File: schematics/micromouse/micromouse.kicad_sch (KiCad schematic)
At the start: 0 parts

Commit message: Update
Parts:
- added J1: TOF_FRONT, Connector_PinHeader_2.54mm:PinHeader_1x06_P2.54mm_Vertical, symbol Connector_Generic:Conn_01x06
- added J2: TOF_LEFT, Connector_PinHeader_2.54mm:PinHeader_1x06_P2.54mm_Vertical, symbol Connector_Generic:Conn_01x06
- added J3: TOF_RIGHT, Connector_PinHeader_2.54mm:PinHeader_1x06_P2.54mm_Vertical, symbol Connector_Generic:Conn_01x06
- added J4: Conn_01x06, Connector_PinHeader_2.54mm:PinHeader_1x06_P2.54mm_Vertical, symbol Connector_Generic:Conn_01x06
- added J5: BatteryConnector, Connector_JST:JST_EH_B2B-EH-A_1x02_P2.50mm_Vertical, symbol Connector_Generic:Conn_01x02
- added U1: STM32F103CBTx, Package_QFP:LQFP-48_7x7mm_P0.5mm, symbol MCU_ST_STM32F1:STM32F103CBTx
- added U2: PMW3360DM-T2QU, PMW3360DM:PMW3360, symbol PMW3360DM:PMW3360DM-T2QU
- added U3: BMI160, Package_LGA:Bosch_LGA-14_3x2.5mm_P0.5mm, symbol Sensor_Motion:BMI160
- added Y1: Crystal, Crystal:Crystal_HC49-4H_Vertical, symbol Device:Crystal
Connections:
- new net: U1.23 (VSS), U1.35 (VSS), U1.47 (VSS)
- new net +3.3V: J1.6 (Pin_6), J2.6 (Pin_6), J3.6 (Pin_6), J4.5 (Pin_5)
- new net GND: J1.5 (Pin_5), J2.5 (Pin_5), J3.5 (Pin_5), J4.4 (Pin_4)
- new net bt_enable: J4.6 (Pin_6)
- new net bt_rx: J4.2 (Pin_2)
- new net bt_state: J4.1 (Pin_1)
- new net bt_tx: J4.3 (Pin_3)
- new net tofF_int: J1.2 (Pin_2)
- new net tofF_scl: J1.3 (Pin_3)
- new net tofF_sda: J1.4 (Pin_4)
- new net tofF_xshut: J1.1 (Pin_1)
- new net tofL_int: J2.2 (Pin_2)
- new net tofL_scl: J2.3 (Pin_3)
- new net tofL_sda: J2.4 (Pin_4)
- new net tofL_xshut: J2.1 (Pin_1)
- new net tofR_int: J3.2 (Pin_2)
- new net tofR_scl: J3.3 (Pin_3)
- new net tofR_sda: J3.4 (Pin_4)
- new net tofR_xshut: J3.1 (Pin_1)

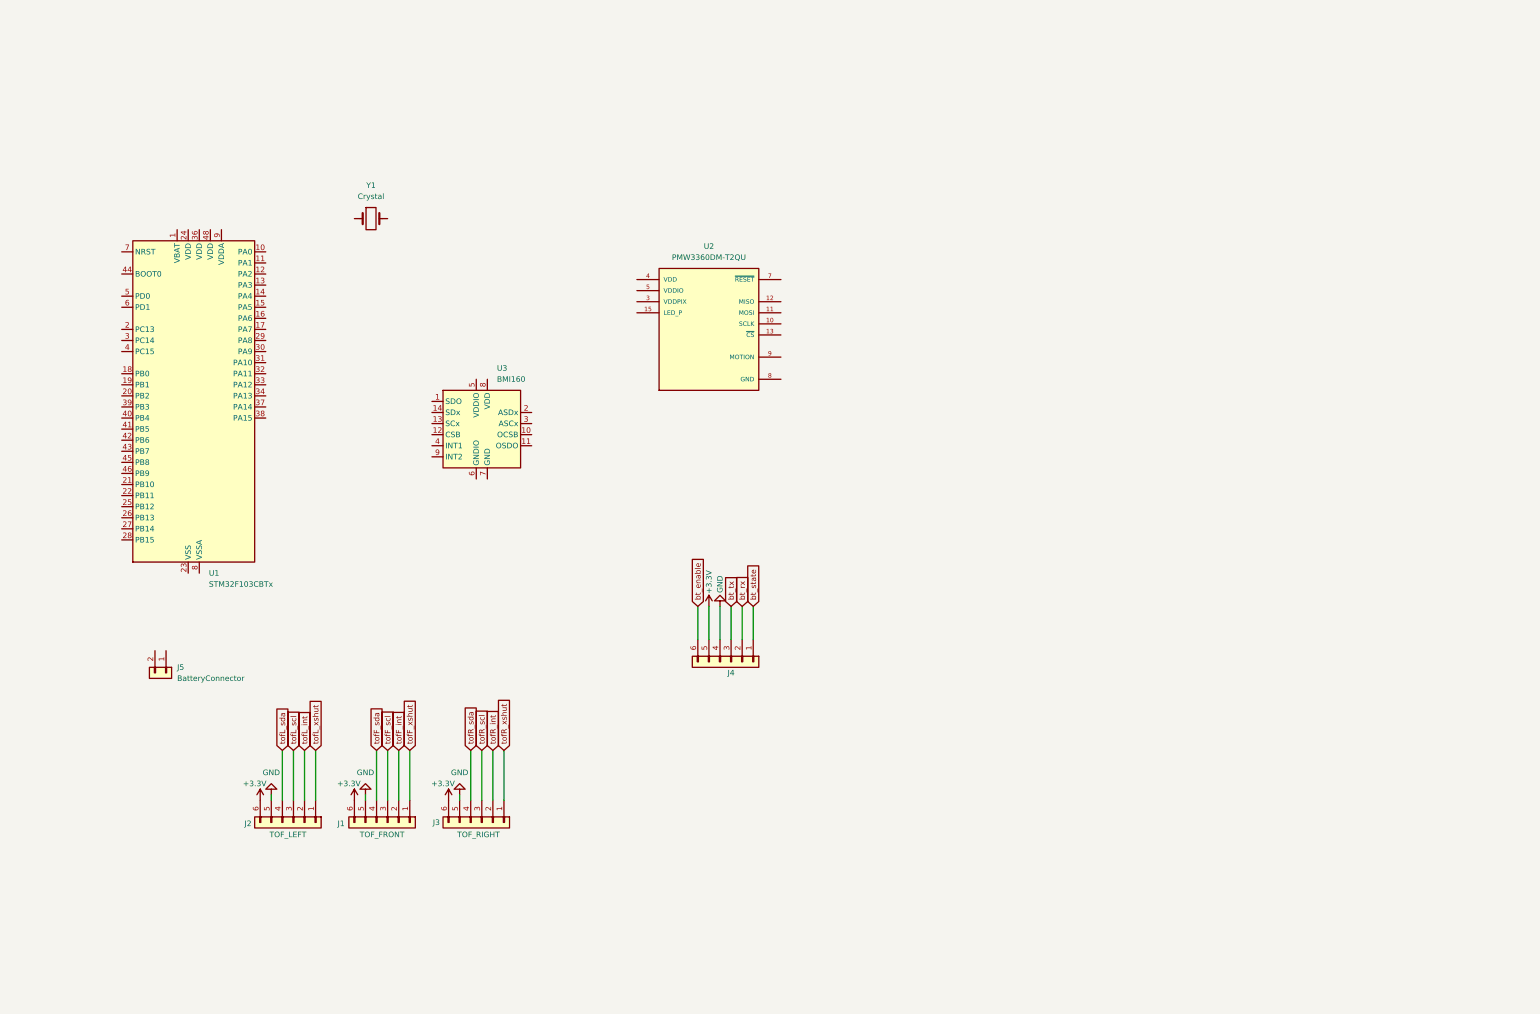
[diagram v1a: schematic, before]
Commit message: Move datasheets, add application note for smt32f103 hardware development Add PCB cut from 3D model (DXF) Reorganize datasheet, add labels and connectors for tofs i2c (x2), add I2C expancer (PCF8574), add mouse sensor (PMW3360) connector and SPI1 labels Added SPI2 labels (may be removed if not used)
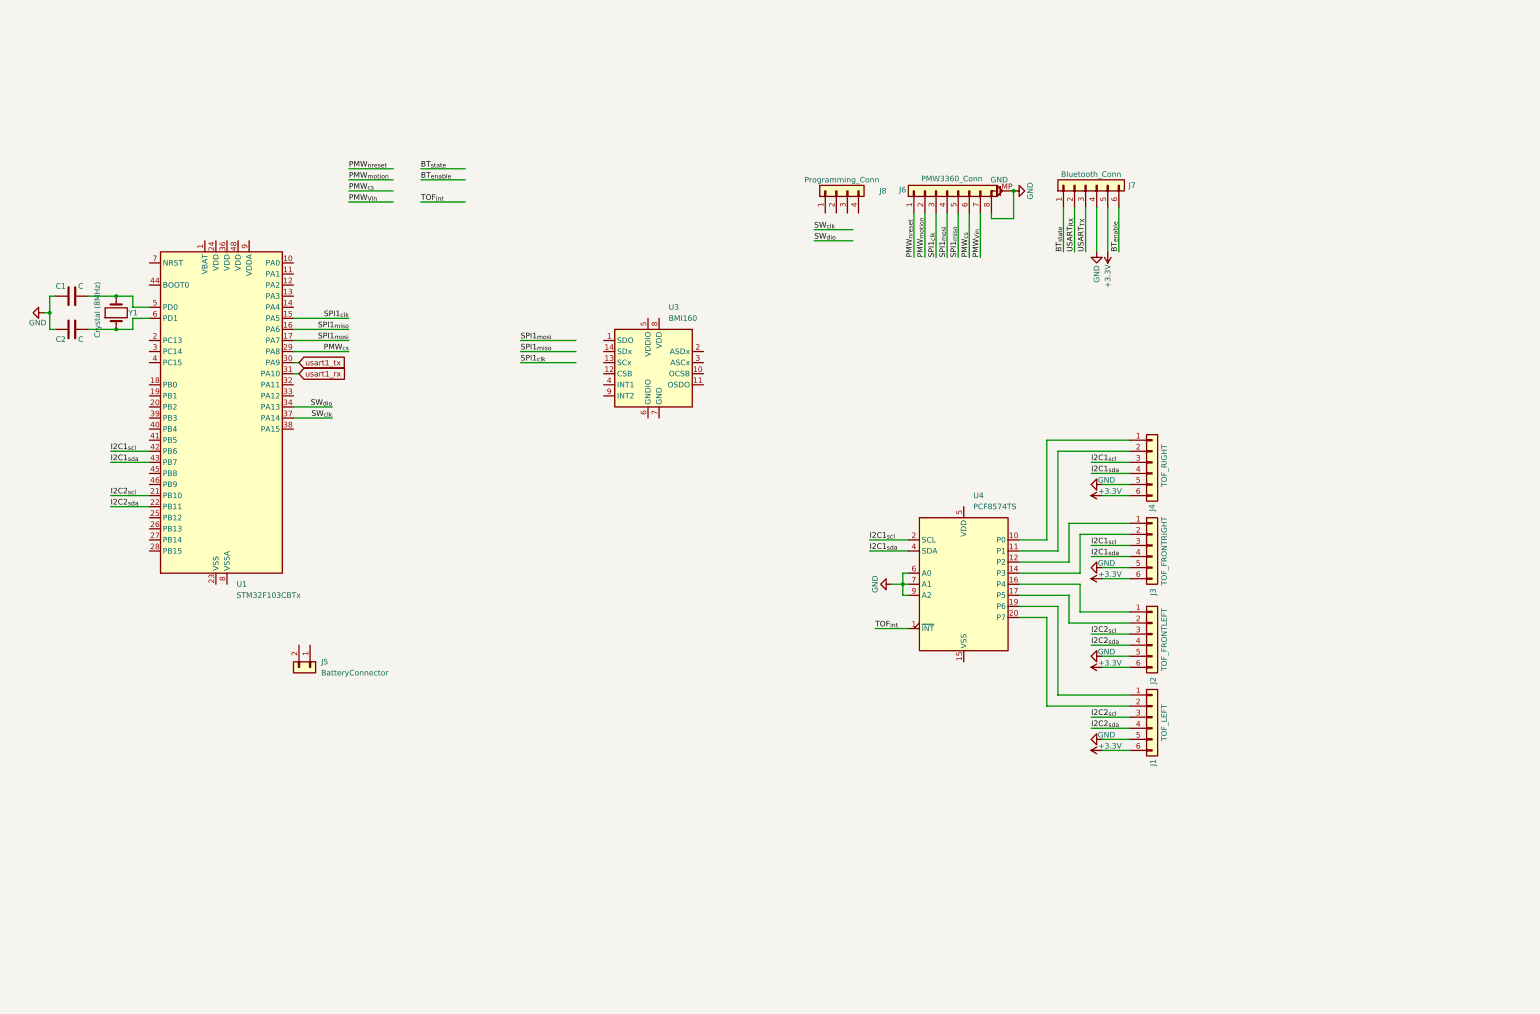
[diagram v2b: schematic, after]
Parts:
- removed U2: PMW3360DM-T2QU, PMW3360DM:PMW3360, symbol PMW3360DM:PMW3360DM-T2QU
- added C1, C2: C, symbol Device:C
- added J3: TOF_FRONTRIGHT, Connector_PinHeader_2.54mm:PinHeader_1x06_P2.54mm_Vertical, symbol Connector_Generic:Conn_01x06
- added J6: PMW3360_Conn, Connector_JST:JST_SH_SM08B-SRSS-TB_1x08-1MP_P1.00mm_Horizontal, symbol Connector_Generic_MountingPin:Conn_01x08_MountingPin
- added J8: Programming_Conn, Connector_PinHeader_2.54mm:PinHeader_1x06_P2.54mm_Vertical, symbol Connector_Generic:Conn_01x04
- added U4: PCF8574TS, Package_SO:SSOP-20_4.4x6.5mm_P0.65mm, symbol Interface_Expansion:PCF8574TS
- J1: value TOF_FRONT -> TOF_LEFT
- J2: value TOF_LEFT -> TOF_FRONTLEFT
- J7: renamed from J4; value Conn_01x06 -> Bluetooth_Conn
- Y1: value Crystal -> Crystal (8MHz)
- renumbered J3 to J4
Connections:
- net tofF_scl is gone; now on net I2C2_{scl}: J1.3 (Pin_3)
- net tofF_sda is gone; now on net I2C2_{sda}: J1.4 (Pin_4)
- net tofL_scl is gone; now on net I2C2_{scl}: J2.3 (Pin_3)
- net tofL_sda is gone; now on net I2C2_{sda}: J2.4 (Pin_4)
- net tofR_scl is gone; now on net I2C1_{scl}: J4.3 (Pin_3)
- net tofR_sda is gone; now on net I2C1_{sda}: J4.4 (Pin_4)
- net +3.3V: now also J3.6 (Pin_6)
- net GND: now also C1.1, C2.2, J3.5 (Pin_5), J6.8 (Pin_8), J6.MP (MountPin), U4.6 (A0), U4.7 (A1), U4.9 (A2)
- net SPI1_{clk}: now reaches U1.15 (PA5)
- net SPI1_{clk}: now also J6.3 (Pin_3)
- net SPI1_{miso}: now reaches U1.16 (PA6)
- net SPI1_{miso}: now also J6.5 (Pin_5)
- net SPI1_{mosi}: now reaches U1.17 (PA7)
- net SPI1_{mosi}: now also J6.4 (Pin_4)
- net I2C2_{scl}: now reaches U1.21 (PB10)
- net I2C2_{sda}: now reaches U1.22 (PB11)
- net PMW_{cs}: now reaches U1.29 (PA8)
- net PMW_{cs}: now also J6.6 (Pin_6)
- net usart1_tx: now reaches U1.30 (PA9)
- net usart1_rx: now reaches U1.31 (PA10)
- net SW_{dio}: now reaches U1.34 (PA13)
- net SW_{clk}: now reaches U1.37 (PA14)
- net I2C1_{scl}: now reaches U1.42 (PB6)
- net I2C1_{scl}: now also J3.3 (Pin_3), U4.2 (SCL)
- net I2C1_{sda}: now reaches U1.43 (PB7)
- net I2C1_{sda}: now also J3.4 (Pin_4), U4.4 (SDA)
- net at U1.5 (PD0): now also Y1.2, C1.2
- net at U1.6 (PD1): now also Y1.1, C2.1
- net bt_enable renamed BT_{enable}
- net bt_rx renamed USART_{RX}
- net bt_state renamed BT_{state}
- net bt_tx renamed USART_{TX}
- net tofF_int: no longer names the net of J1.2 (Pin_2)
- net tofF_int: now also U4.20 (P7)
- net tofF_xshut: no longer names the net of J1.1 (Pin_1)
- net tofF_xshut: now also U4.19 (P6)
- net tofL_int: no longer names the net of J2.2 (Pin_2)
- net tofL_int: now also U4.17 (P5)
- net tofL_xshut: no longer names the net of J2.1 (Pin_1)
- net tofL_xshut: now also U4.16 (P4)
- net tofR_int: no longer names the net of J4.2 (Pin_2)
- net tofR_int: now also U4.11 (P1)
- net tofR_xshut: no longer names the net of J4.1 (Pin_1)
- net tofR_xshut: now also U4.10 (P0)
- new net: J3.1 (Pin_1), U4.12 (P2)
- new net: J3.2 (Pin_2), U4.14 (P3)
- new net PMW_{Vin}: J6.7 (Pin_7)
- new net PMW_{motion}: J6.2 (Pin_2)
- new net PMW_{nreset}: J6.1 (Pin_1)
- new net TOF_{int}: U4.1 (~{INT})
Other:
- moved on the sheet: J4, J5, J7, U1, U3, Y1

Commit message: Reorganize again... add things
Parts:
- removed U3: BMI160, Package_LGA:Bosch_LGA-14_3x2.5mm_P0.5mm, symbol Sensor_Motion:BMI160
- added D1: LED, symbol Device:LED
- added H1, H2, H3, H4: MountingHole_Pad, MountingHole:MountingHole_2.2mm_M2_ISO14580_Pad, symbol Mechanical:MountingHole_Pad
- added J10: MotorB_Conn, Connector_JST:JST_EH_B2B-EH-A_1x02_P2.50mm_Vertical, symbol Connector_Generic:Conn_01x02
- added J11: BMI_ConnB, Connector_PinHeader_2.54mm:PinHeader_1x07_P2.54mm_Vertical, symbol Connector_Generic:Conn_01x07
- added J12: BMI_ConnA, Connector_PinHeader_2.54mm:PinHeader_1x05_P2.54mm_Vertical, symbol Connector_Generic:Conn_01x05
- added J9: MotorA_Conn, Connector_JST:JST_EH_B2B-EH-A_1x02_P2.50mm_Vertical, symbol Connector_Generic:Conn_01x02
- added SW1: SW_Push, symbol Switch:SW_Push
- added SW2: SW_SPDT, symbol Switch:SW_SPDT
- added U2: DRV8833PWP, Package_SO:HTSSOP-16-1EP_4.4x5mm_P0.65mm_EP3.4x5mm_Mask2.46x2.31mm_ThermalVias, symbol Driver_Motor:DRV8833PWP
- C1, C2: footprint (none) -> Capacitor_SMD:C_0805_2012Metric_Pad1.18x1.45mm_HandSolder
- J6: footprint Connector_JST:JST_SH_SM08B-SRSS-TB_1x08-1MP_P1.00mm_Horizontal -> Connector_JST:JST_SH_BM08B-SRSS-TB_1x08-1MP_P1.00mm_Vertical
- J8: footprint Connector_PinHeader_2.54mm:PinHeader_1x06_P2.54mm_Vertical -> Connector_PinHeader_2.54mm:PinHeader_1x04_P2.54mm_Vertical
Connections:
- net PMW_{Vin} is gone; now on net VCC_{3.3}: J6.7 (Pin_7)
- net GND: now also U4.15 (VSS), H1.1, H2.1, H3.1, H4.1, J11.3 (Pin_3), U2.13 (GND), U2.17 (GND)
- net SPI1_{clk}: now also J11.4 (Pin_4)
- net SPI1_{miso}: now also J11.7 (Pin_7)
- net SPI1_{mosi}: now also J11.5 (Pin_5)
- net +3.3V renamed VCC_{3.3}
- net VCC_{3.3}: now also J11.1 (Pin_1)
- net usart1_rx renamed USART1_{RX}
- net usart1_tx renamed USART1_{TX}
- new net: J9.1 (Pin_1), U2.2 (AOUT1)
- new net: J9.2 (Pin_2), U2.4 (AOUT2)
- new net: J10.2 (Pin_2), U2.5 (BOUT2)
- new net: J10.1 (Pin_1), U2.7 (BOUT1)
- new net BMI_{cs}: J11.6 (Pin_6)
- new net BMI_{int1}: J12.3 (Pin_3)
- new net BMI_{int2}: J12.2 (Pin_2)
- new net MOTOR_{a1}: U2.16 (AIN1)
- new net MOTOR_{a2}: U2.15 (AIN2)
- new net MOTOR_{aen}: U2.3 (AISEN)
- new net MOTOR_{b1}: U2.9 (BIN1)
- new net MOTOR_{b2}: U2.10 (BIN2)
- new net MOTOR_{ben}: U2.6 (BISEN)
- new net MOTOR_{fault}: U2.8 (~{FAULT})
- new net MOTOR_{sleep}: U2.1 (~{SLEEP})
- new net VCC_{6}: U2.12 (VM)
- no-connect marks 0 -> 4
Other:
- note added: "PMW3360 Mounting Holes"
- moved on the sheet: J1, J2, J3, J4, J5

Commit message: Schamatic status update: * STM32 with external clock, DebugPort and communication lines (SPI1, I2C0 and I2C1) * First version of power supply schematic [TODO: Check possible short circuit] * Motor controller schematic * Mouse sensor connector + mounting holes * Bluetooth connector for HC-05/HC-06 * TOF schematic using GPIO expander * BMI160 Mounting holes
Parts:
- added C3: 0.01uF, Capacitor_SMD:C_0805_2012Metric_Pad1.18x1.45mm_HandSolder, symbol Device:C
- added C4: 10uF, Capacitor_SMD:C_0805_2012Metric_Pad1.18x1.45mm_HandSolder, symbol Device:C
- added C5: 2.2uF, Capacitor_SMD:C_0805_2012Metric_Pad1.18x1.45mm_HandSolder, symbol Device:C
- added J13: StepDown_{In+}, Connector_PinHeader_2.54mm:PinHeader_1x01_P2.54mm_Vertical, symbol Connector_Generic:Conn_01x01
- added J14: StepDown_{In-}, Connector_PinHeader_2.54mm:PinHeader_1x01_P2.54mm_Vertical, symbol Connector_Generic:Conn_01x01
- added J15: StepDown_{Out+}, Connector_PinHeader_2.54mm:PinHeader_1x01_P2.54mm_Vertical, symbol Connector_Generic:Conn_01x01
- added J16: StepDown_{Out-}, Connector_PinHeader_2.54mm:PinHeader_1x01_P2.54mm_Vertical, symbol Connector_Generic:Conn_01x01
- added R1: R, Resistor_SMD:R_0805_2012Metric_Pad1.20x1.40mm_HandSolder, symbol Device:R
- added R2, R3: 200m, Resistor_SMD:R_0805_2012Metric_Pad1.20x1.40mm_HandSolder, symbol Device:R
- added U3: AMS1117-3.3, Package_TO_SOT_SMD:SOT-223-3_TabPin2, symbol Regulator_Linear:AMS1117-3.3
- D1: footprint (none) -> LED_SMD:LED_0805_2012Metric_Pad1.15x1.40mm_HandSolder
- H1: now in the parts list
- SW1: footprint (none) -> Button_Switch_SMD:SW_SPST_PTS645
- SW2: footprint (none) -> Button_Switch_THT:SW_Slide_SPDT_Straight_CK_OS102011MS2Q
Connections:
- net GND: now also J5.1 (Pin_1), SW2.3 (C), C4.2, C5.2, J14.1 (Pin_1), J16.1 (Pin_1), R1.1, R2.1, R3.1, U3.1 (GND)
- net VCC_{3.3}: now also D1.1 (K), U4.5 (VDD), R1.2
- net at U2.11 (VCP): now also C3.1
- net at U2.14 (VINT): now also C5.1
- net at SW2.1 (A): now also U3.3 (VI)
- net VCC_{5}: now reaches SW2.2 (B)
- net VCC_{5}: now also J15.1 (Pin_1)
- net at D1.2 (A): now also U3.2 (VO)
- net VCC_{7.4}: now reaches J5.2 (Pin_2)
- net VCC_{7.4}: now also J13.1 (Pin_1)
- net MOTOR_{aen}: no longer names the net of U2.3 (AISEN)
- net MOTOR_{aen}: now also R2.2
- net MOTOR_{ben}: no longer names the net of U2.6 (BISEN)
- net MOTOR_{ben}: now also R3.2
- net VCC_{6} renamed VCC_{7,4}
- net VCC_{7,4}: now also C3.2, C4.1
- no-connect marks 4 -> 6
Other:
- note added: "BMI160 Mounting Holes"
- note added: "Bluetooth"
- note added: "Motor driver"
- note added: "Mouse sensor"
- note added: "Stepdown Mounting Holes"
- note added: "TOF sensors"
- moved on the sheet: D1, J11, J12, J5, J8, SW1
